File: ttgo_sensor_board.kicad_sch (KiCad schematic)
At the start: 59 parts, among them J1 Conn_01x13_Female, J2 Conn_01x13_Female, J3 Conn_01x03_Female, J4 Conn_01x03_Female, J5 Conn_01x04_Female, J6 Conn_01x04_Female, J7 Conn_01x04_Female, Q1 Q_NMOS_GSD, Q2 Q_NMOS_GSD, U1 BME680, U2 TCA9800, U3 TLV70218_SOT23-5, U4 LSM6DS3, U5 VEML7700

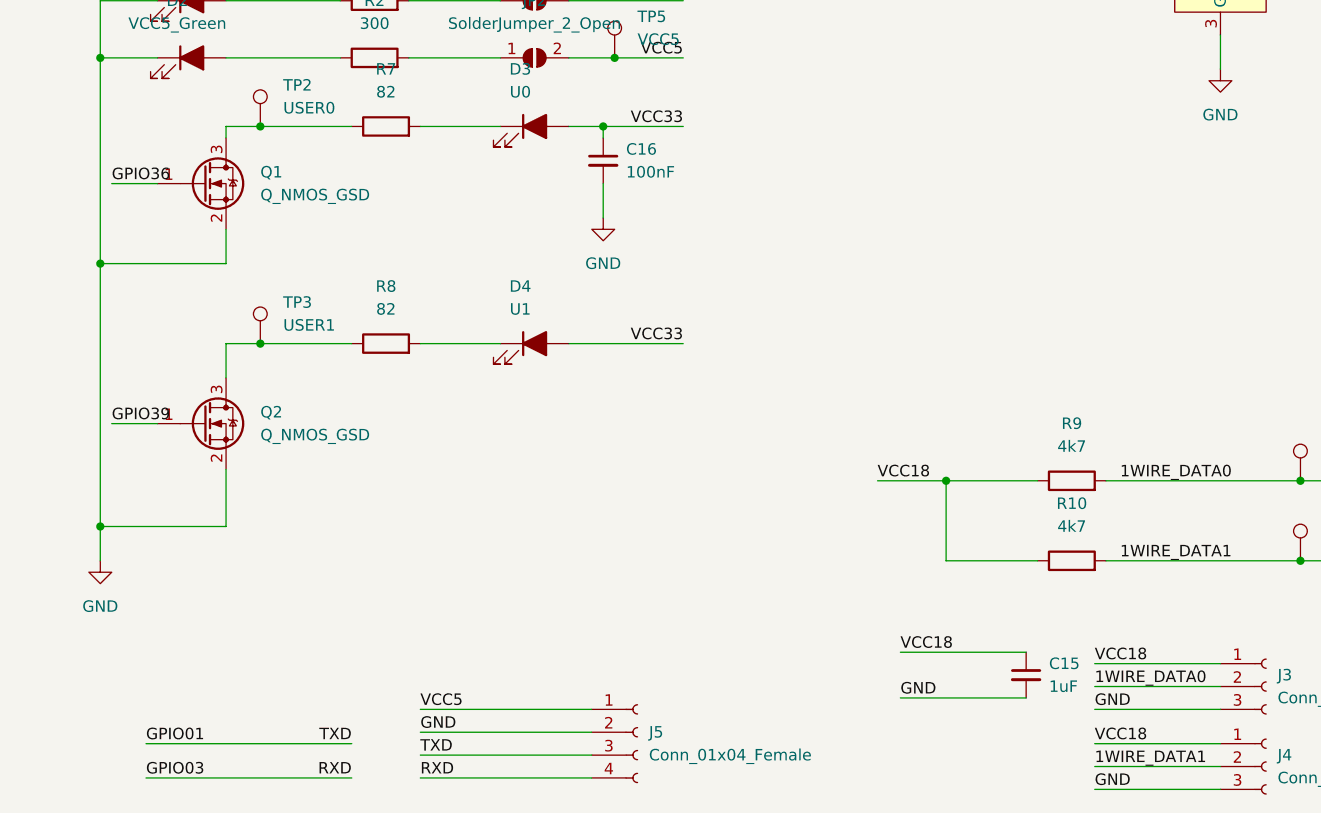
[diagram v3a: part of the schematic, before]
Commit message: fix schematic after first prototype
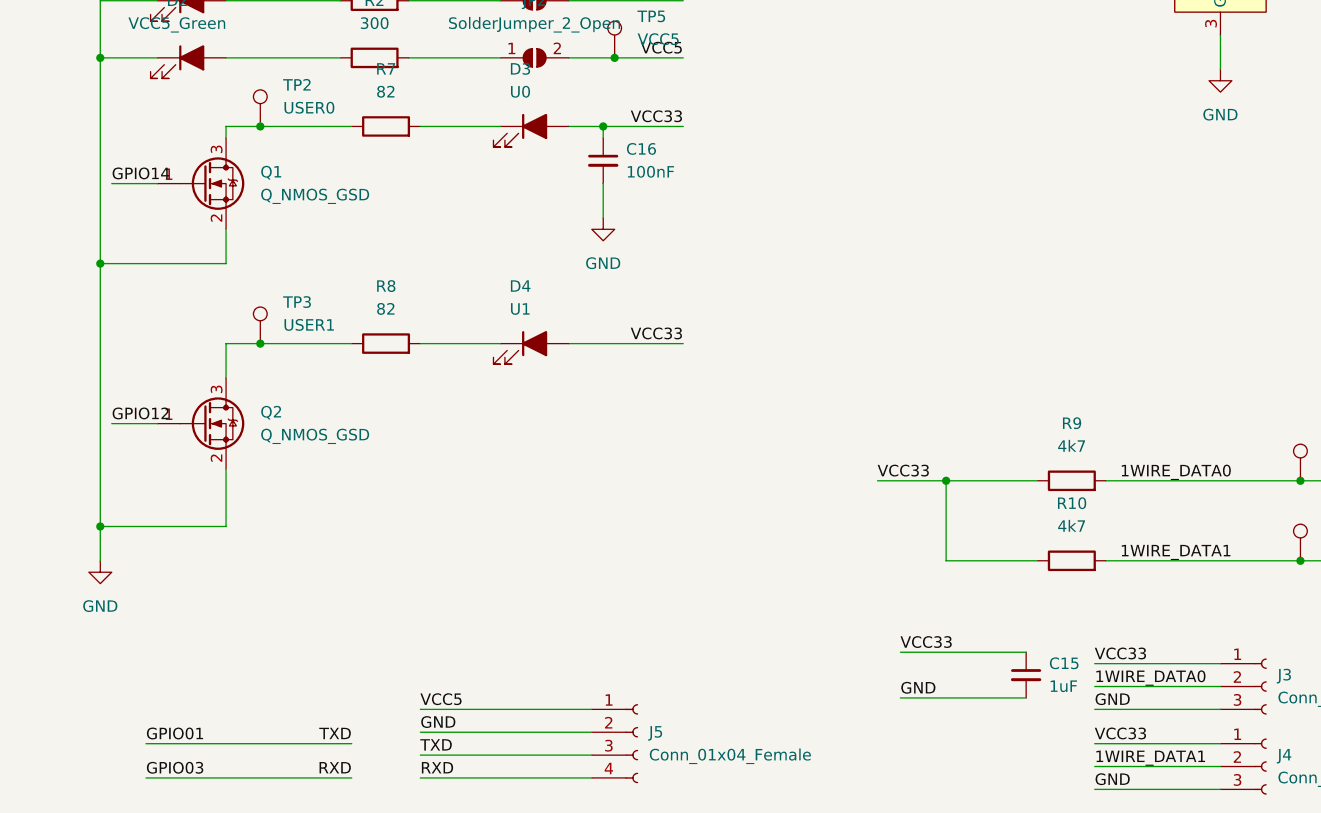
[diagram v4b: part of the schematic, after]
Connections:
- net GPIO12: now also Q2.1 (G)
- net GPIO14: now also Q1.1 (G)
- net GPIO36: no longer Q1.1 (G)
- net GPIO39: no longer Q2.1 (G)
- net VCC18: no longer C15.1, J3.1 (Pin_1), J4.1 (Pin_1), R10.1, R9.1
- net VCC33: now also C15.1, J3.1 (Pin_1), J4.1 (Pin_1), R10.1, R9.1
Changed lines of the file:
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@@
     (effects (font (size 1.27 1.27)) (justify left bottom))
   )
-  (label "VCC18" (at 111.76 176.53 0)
+  (label "VCC33" (at 111.76 176.53 0)
     (effects (font (size 1.27 1.27)) (justify left bottom))
   )
@@
     (effects (font (size 1.27 1.27)) (justify left bottom))
   )
-  (label "VCC18" (at 133.35 177.8 0)
+  (label "VCC33" (at 133.35 177.8 0)
     (effects (font (size 1.27 1.27)) (justify left bottom))
   )
@@
     (effects (font (size 1.27 1.27)) (justify left bottom))
   )
-  (label "GPIO39" (at 24.13 151.13 0)
+  (label "GPIO12" (at 24.13 151.13 0)
     (effects (font (size 1.27 1.27)) (justify left bottom))
   )
@@
     (effects (font (size 1.27 1.27)) (justify right bottom))
   )
-  (label "VCC18" (at 109.22 157.48 0)
+  (label "VCC33" (at 109.22 157.48 0)
     (effects (font (size 1.27 1.27)) (justify left bottom))
   )
@@
     (effects (font (size 1.27 1.27)) (justify right bottom))
   )
-  (label "GPIO36" (at 24.13 124.46 0)
+  (label "GPIO14" (at 24.13 124.46 0)
     (effects (font (size 1.27 1.27)) (justify left bottom))
   )
@@
     (effects (font (size 1.27 1.27)) (justify right bottom))
   )
-  (label "VCC18" (at 133.35 186.69 0)
+  (label "VCC33" (at 133.35 186.69 0)
     (effects (font (size 1.27 1.27)) (justify left bottom))
   )
